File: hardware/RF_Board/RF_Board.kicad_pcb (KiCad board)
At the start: 4 copper layers, 90 x 90 mm, 130 parts, among them J1 Conn_Coaxial, J2 Conn_01x04_Male, J3 Conn_Coaxial, J4 Conn_01x04_Male, J5 Conn_01x06_Female, J6 Conn_01x06_Female, J7 Conn_01x06_Female, J8 L77TSAH15SOL2RM8, J9 Conn_01x09_Male, Q1 2N7002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

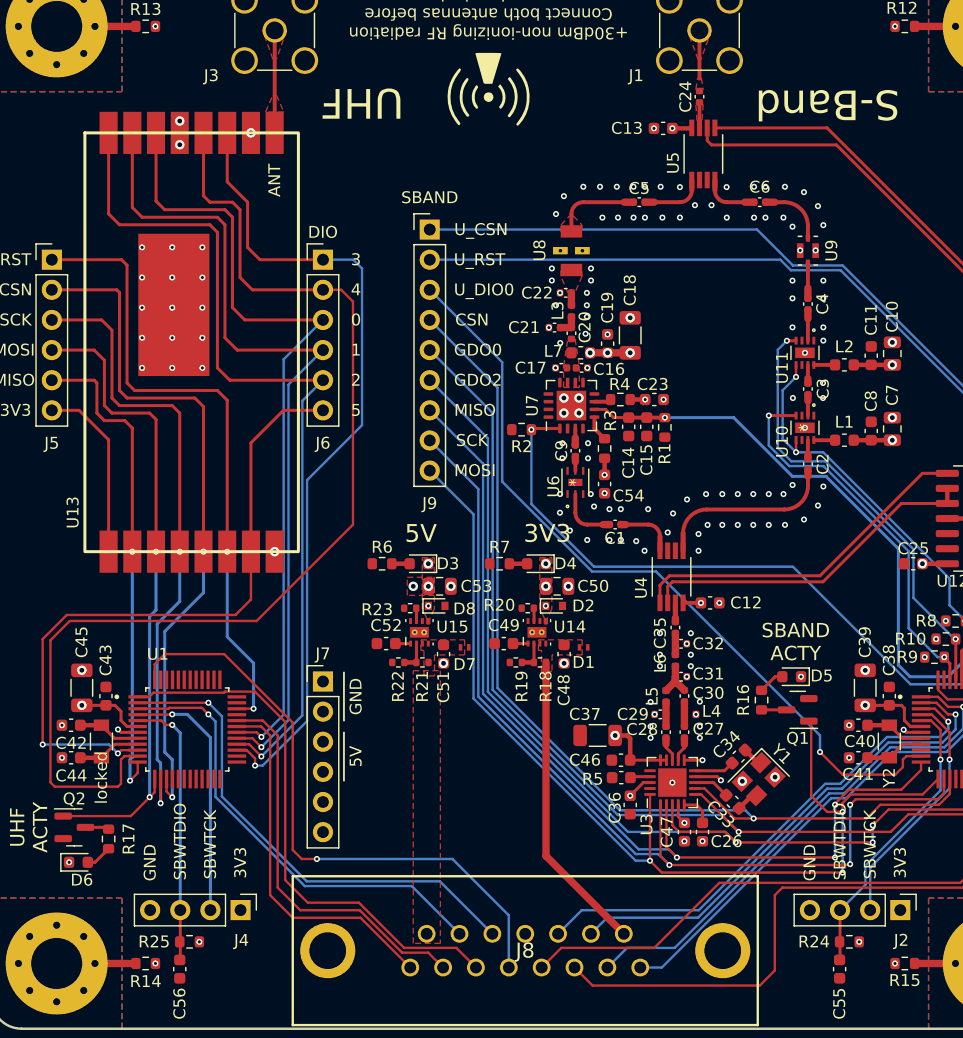
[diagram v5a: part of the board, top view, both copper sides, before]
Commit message: fix all DRC issues and generate gerbers
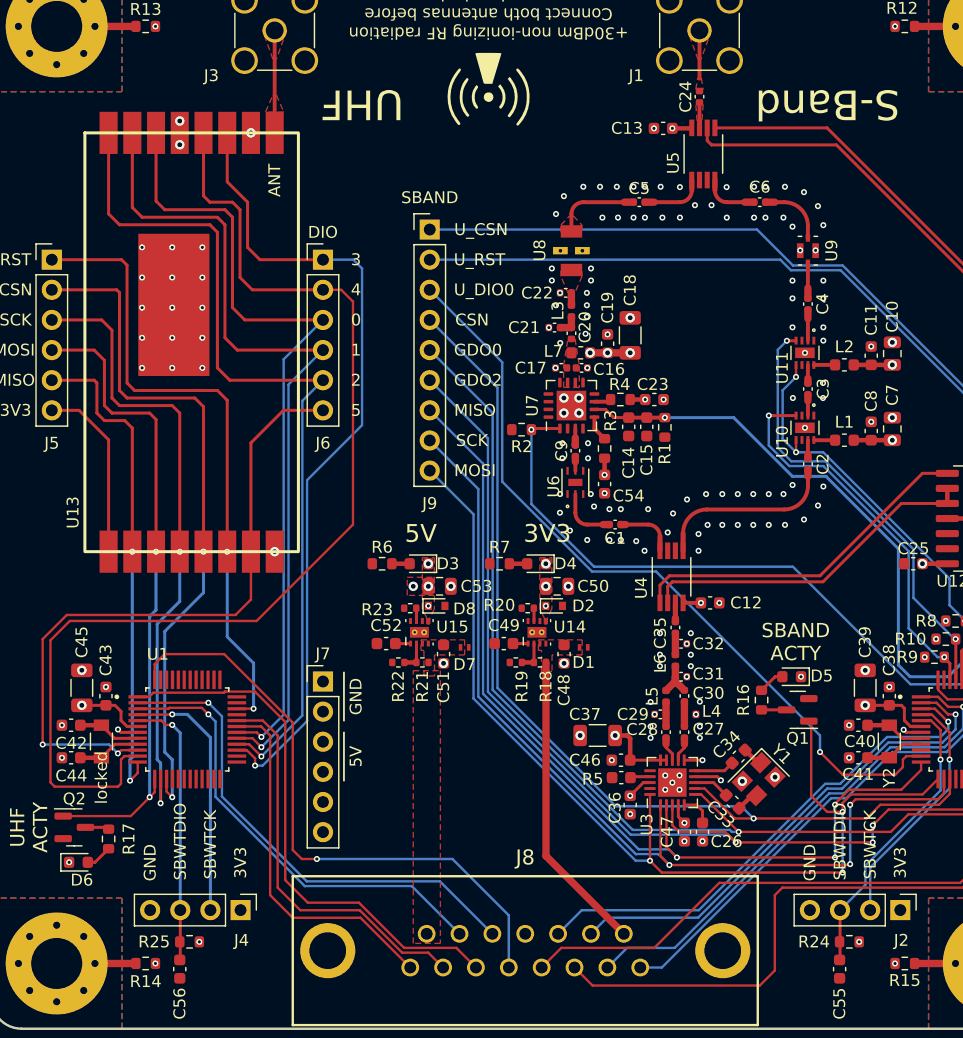
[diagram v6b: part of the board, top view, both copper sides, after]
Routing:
- net GND: vias 162 -> 173
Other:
- board text added: "5V0"
- board text added: "RX"
- board text added: "RX E"
- board text added: "RX O"
- board text added: "TX"
- board text added: "TX E"
- board text added: "TX O"
